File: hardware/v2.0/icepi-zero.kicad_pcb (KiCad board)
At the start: 4 copper layers, 65 x 30 mm, 202 parts, among them IC1 IS42S16160J-6BLI, IC2 LTC2256CUJ-12#PBF, J1 Conn_02x20_Counter_Clockwise, J2 GPDI_C_1.3, J3 USB_C_Receptacle_USB2.0_14P, J4 USB_C_Receptacle_USB2.0_14P, J5 USB_C_Receptacle_USB2.0_14P, J6 Micro_SD_Card_Det2, J7 RSP-122811-01, SW1 SW_Push, SW2 SW_Push, U1 ECP5U-25F-CABGA256, U10 TPD2EUSB30A, U11 LT1993CUD-2_PBF, U12 W25Q128JVS, U13 TCR5FM50A, U2 LTC3407AEDD-2_PBF, U3 TLV62569DBV, U5 TCR5FM18A, U6 PCA9306DC1, U7 TPD2EUSB30A, U8 TPD2EUSB30A, U9 FT231XQ, Y1 SG-8018CG 50.000000MHz, Y2 SG-8018CG 25.000000MHz

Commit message: External ADC finalization
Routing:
- net /Flash/FLASH_MOSI: track 8.92 -> 9.53 mm
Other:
- board text added: "Icepi Zero v2.3"
- board text removed: "Icepi Zero v2.0"

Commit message: Minor fixes
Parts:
- moved C75 0.58 mm to (171.9, 108.1)
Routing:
- net +3V3: track 126.9 -> 125.7 mm
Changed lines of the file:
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@@
 			(layers "F.Cu")
 			(net 15 "GND")
-			(pinfunction "CENTER")
-			(pintype "bidirectional")
+			(pinfunction "GND")
+			(pintype "power_in")
 			(options
 				(clearance outline)
@@
 	(footprint "Capacitor_SMD:C_0402_1005Metric"
 		(layer "B.Cu")
-		(at 171.4 107.75 -90)
+		(at 171.86 108.1 -90)
 		(descr "Capacitor SMD 0402 (1005 Metric), square (rectangular) end terminal, IPC-7351 nominal, (Body size source: IPC-SM-782 page 76, https://www.pcb-3d.com/wordpress/wp-content/uploads/ipc-sm-782a_amendment_1_and_2.pdf), generated with kicad-footprint-generator")
 		(tags "capacitor")
@@
 	)
 	(segment
-		(start 152.33 106.4)
-		(end 152.24 106.4)
-		(width 0.17)
-		(layer "F.Cu")
-		(net 18)
-	)
-	(segment
 		(start 175.152666 97.28)
 		(end 175.15 97.277334)
@@
 	)
 	(segment
+		(start 152.16 106.35)
+		(end 152.16 106.11)
+		(width 0.17)
+		(layer "F.Cu")
+		(net 18)
+	)
+	(segment
 		(start 148.8 106.75)
 		(end 148.64 106.91)
@@
 	)
 	(segment
-		(start 152.16 106.59)
-		(end 152.16 106.57)
-		(width 0.17)
-		(layer "F.Cu")
-		(net 18)
-	)
-	(segment
-		(start 152.24 106.4)
-		(end 152.16 106.32)
-		(width 0.17)
-		(layer "F.Cu")
-		(net 18)
-	)
-	(segment
 		(start 146.809 103.20996)
 		(end 147.029508 103.20996)
@@
 	)
 	(segment
-		(start 152.39 106.34)
-		(end 152.33 106.4)
-		(width 0.17)
-		(layer "F.Cu")
-		(net 18)
-	)
-	(segment
 		(start 166.31 107.93)
 		(end 166.31 107.511155)
@@
 	)
 	(segment
-		(start 152.16 106.57)
-		(end 152.39 106.34)
-		(width 0.17)
-		(layer "F.Cu")
-		(net 18)
-	)
-	(segment
 		(start 119.775001 110.725001)
 		(end 119.775 110.725)
@@
 	)
 	(segment
-		(start 152.16 106.59)
-		(end 152.16 106.32)
-		(width 0.17)
-		(layer "F.Cu")
-		(net 18)
-	)
-	(segment
 		(start 179.31 103.07)
 		(end 179.49 102.89)
@@
 	)
 	(segment
+		(start 153.95 106.35)
+		(end 152.16 106.35)
+		(width 0.17)
+		(layer "F.Cu")
+		(net 18)
+	)
+	(segment
 		(start 150.313701 107.13)
 		(end 150.321605 107.137904)
@@
 	)
 	(segment
-		(start 152 105.95)
-		(end 152.39 106.34)
-		(width 0.17)
-		(layer "F.Cu")
-		(net 18)
-	)
-	(segment
 		(start 151.987904 106.75)
 		(end 151.6 107.137904)
@@
 	)
 	(segment
-		(start 152.39 106.34)
-		(end 153.97 106.34)
-		(width 0.17)
-		(layer "F.Cu")
-		(net 18)
-	)
-	(segment
 		(start 149.543056 102.807913)
 		(end 149.543056 102.806944)
@@
 	)
 	(segment
-		(start 152.16 106.32)
-		(end 152.16 106.11)
-		(width 0.17)
-		(layer "F.Cu")
-		(net 18)
-	)
-	(segment
 		(start 150.39 102.75)
 		(end 150.01 102.37)
@@
 	)
 	(segment
+		(start 153.965 106.365)
+		(end 153.95 106.35)
+		(width 0.17)
+		(layer "F.Cu")
+		(net 18)
+	)
+	(segment
 		(start 152.16 102.91)
 		(end 152 102.75)
@@
 	)
 	(via
-		(at 153.97 106.34)
+		(at 153.965 106.365)
 		(size 0.4)
 		(drill 0.2)
@@
 	)
 	(segment
-		(start 154.565555 106.906)
-		(end 155.034445 106.906)
-		(width 0.4)
-		(layer "B.Cu")
-		(net 18)
-	)
-	(segment
 		(start 120.51 102.475)
 		(end 120.79 102.195)
@@
 	)
 	(segment
-		(start 153.999555 106.34)
-		(end 154.565555 106.906)
-		(width 0.4)
-		(layer "B.Cu")
-		(net 18)
-	)
-	(segment
-		(start 154 106.31)
-		(end 153.97 106.34)
-		(width 0.4)
-		(layer "B.Cu")
-		(net 18)
-	)
-	(segment
 		(start 147.58 107.78)
 		(end 147.65 107.85)
@@
 	)
 	(segment
+		(start 154 106.33)
+		(end 154 106.31)
+		(width 0.4)
+		(layer "B.Cu")
+		(net 18)
+	)
+	(segment
 		(start 140.65 107.2)
 		(end 140.52 107.33)
@@
 	)
 	(segment
+		(start 154.565555 106.906)
+		(end 155.034445 106.906)
+		(width 0.4)
+		(layer "B.Cu")
+		(net 18)
+	)
+	(segment
 		(start 165.97 105.09)
 		(end 166.62 105.09)
@@
 	)
 	(segment
+		(start 154.01 106.41)
+		(end 154.069555 106.41)
+		(width 0.4)
+		(layer "B.Cu")
+		(net 18)
+	)
+	(segment
 		(start 138.94 97.818828)
 		(end 138.661905 97.540733)
@@
 	)
 	(segment
-		(start 165.22 107.53)
-		(end 165.296 107.606)
-		(width 0.5)
+		(start 154.069555 106.41)
+		(end 154.565555 106.906)
+		(width 0.4)
 		(layer "B.Cu")
 		(net 18)
 	)
 	(segment
-		(start 153.97 106.34)
-		(end 153.999555 106.34)
-		(width 0.4)
+		(start 165.22 107.53)
+		(end 165.296 107.606)
+		(width 0.5)
 		(layer "B.Cu")
 		(net 18)
@@
 	)
 	(segment
+		(start 153.965 106.365)
+		(end 154 106.33)
+		(width 0.4)
+		(layer "B.Cu")
+		(net 18)
+	)
+	(segment
 		(start 146.803793 103.213754)
 		(end 146.730039 103.14)
@@
 	)
 	(segment
+		(start 153.965 106.365)
+		(end 154.01 106.41)
+		(width 0.4)
+		(layer "B.Cu")
+		(net 18)
+	)
+	(segment
 		(start 145.26 104.73)
 		(end 145.26 104.92)
@@
 	(segment
 		(start 152.01 99.762149)
-		(end 152.01 99.76)
-		(width 0.17)
-		(layer "B.Cu")
-		(net 42)
-	)
-	(segment
-		(start 152.01 99.762149)
 		(end 153.582149 98.19)
 		(width 0.17)
@@
 	)
 	(segment
-		(start 154 98.61)
-		(end 154.01 98.6)
-		(width 0.17)
-		(layer "F.Cu")
-		(net 195)
-	)
-	(segment
 		(start 163.23 100.39)
 		(end 163.5 100.66)
@@
 		(polygon
 			(pts
-				(xy 152.75 106.65) (xy 148 106.65) (xy 147.98 105.95) (xy 144.48 105.91) (xy 141.17 104.03) (xy 131.47 103.98)
-				(xy 131.5 105.75) (xy 128.5 105.75) (xy 128.52 101.77) (xy 141.73 101.8) (xy 146.2 103.69) (xy 147.47 103.7)
-				(xy 148.75 103.75) (xy 149.75 103.75) (xy 149.75 102.75) (xy 152.75 102.75)
+				(xy 152.76 105.81) (xy 152.2 105.81) (xy 152.200005 106.638742) (xy 147.98 106.63) (xy 147.98 105.95)
+				(xy 144.48 105.91) (xy 141.17 104.03) (xy 131.47 103.98) (xy 131.5 105.75) (xy 128.5 105.75) (xy 128.52 101.77)
+				(xy 141.73 101.8) (xy 146.2 103.69) (xy 147.47 103.7) (xy 148.75 103.75) (xy 149.75 103.75) (xy 149.75 102.75)
+				(xy 152.75 102.75)
 			)
 		)

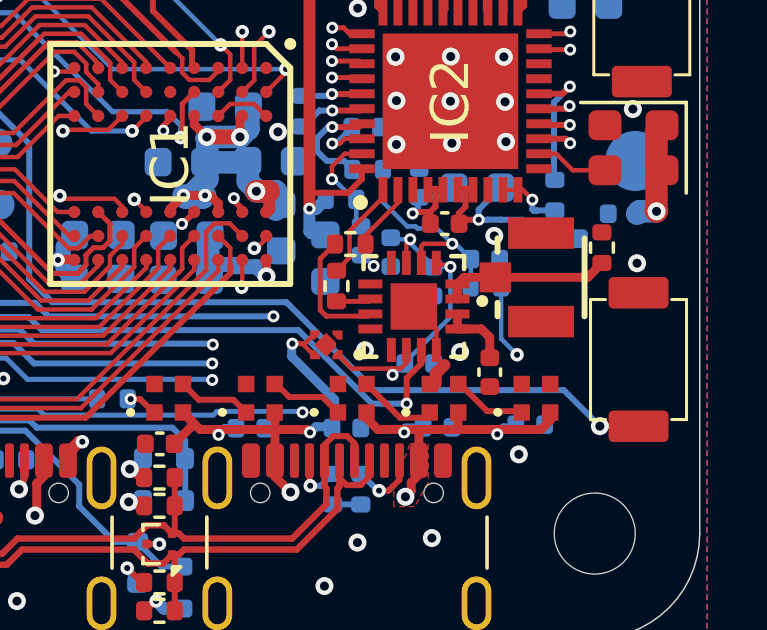
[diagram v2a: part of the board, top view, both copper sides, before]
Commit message: ADC driver power pins bypass
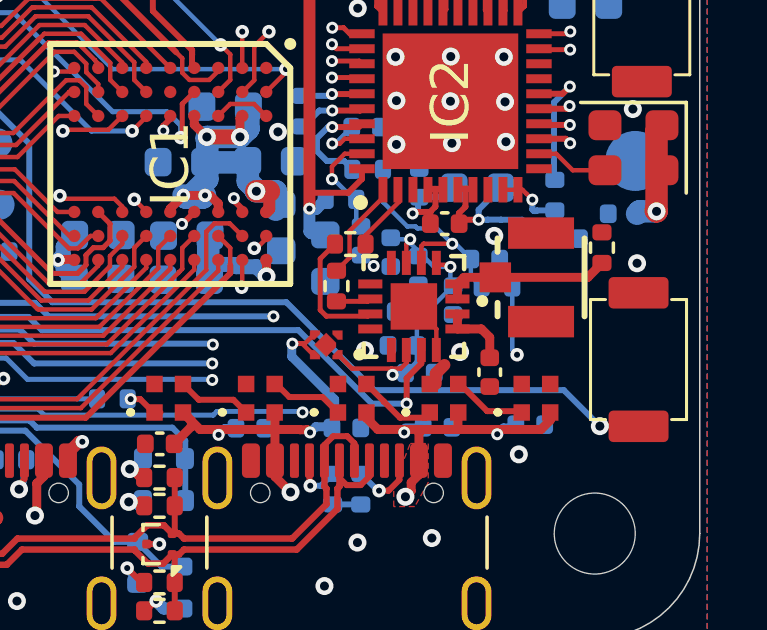
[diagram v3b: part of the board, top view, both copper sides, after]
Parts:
- added C79: 1n, Capacitor_SMD:C_0402_1005Metric, B.Cu at (171.4, 111.2)
- added C80: 1n, Capacitor_SMD:C_0402_1005Metric, B.Cu at (171.4, 107.7)
- added C81: 1n, Capacitor_SMD:C_0402_1005Metric, B.Cu at (172.5, 108.7)
- moved C75 1.27 mm to (171.1, 109.1), turned to 180 degrees
- moved C76 0.82 mm to (170.8, 110.2), turned to 180 degrees
- moved R2 0.37 mm to (174.0, 108.3)
